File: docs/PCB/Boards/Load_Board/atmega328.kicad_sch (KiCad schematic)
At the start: 18 parts, among them J89 Conn_02x10_Odd_Even, J90 AVR-ISP-6, J91 Conn_02x10_Odd_Even, J92 Conn_01x10_Pin, J93 Conn_01x10_Pin, SW2 Tact Switch 6x6mm / 13mm, U2 ATmega328P-P, Y4 Crystal

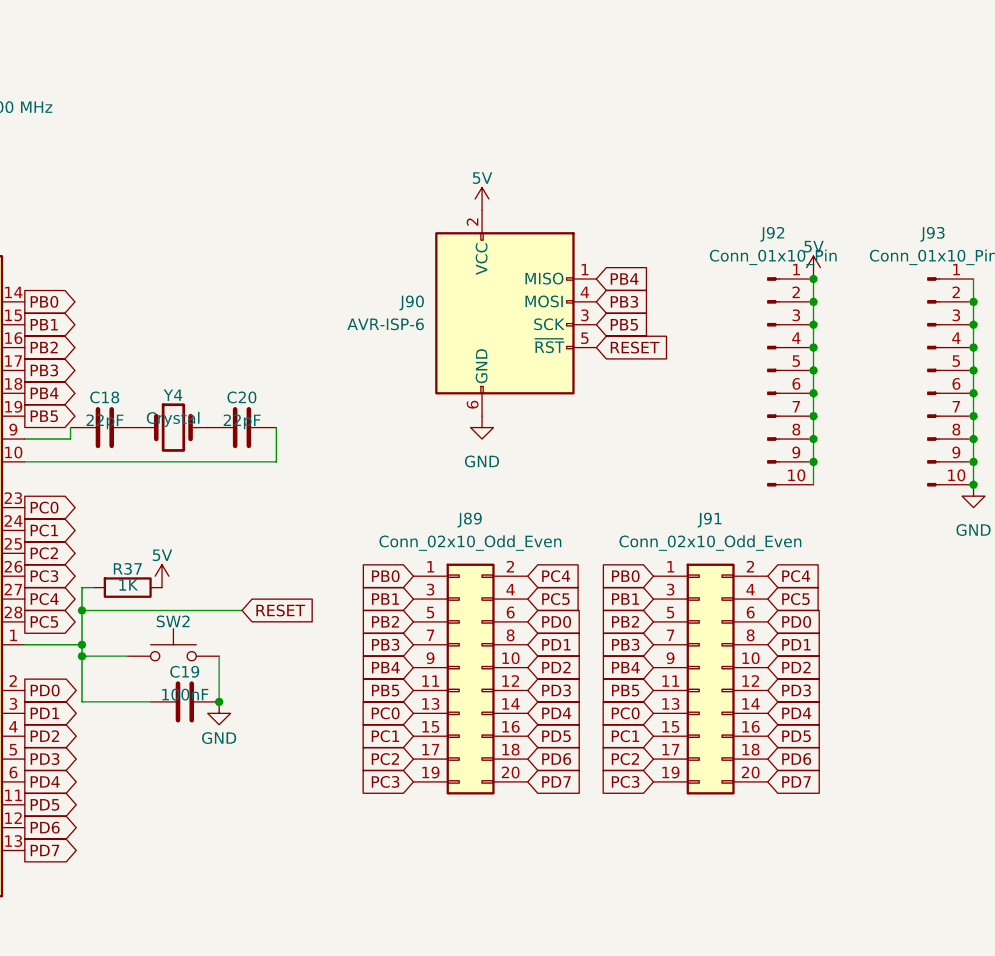
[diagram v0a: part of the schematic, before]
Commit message: Load Board updated.
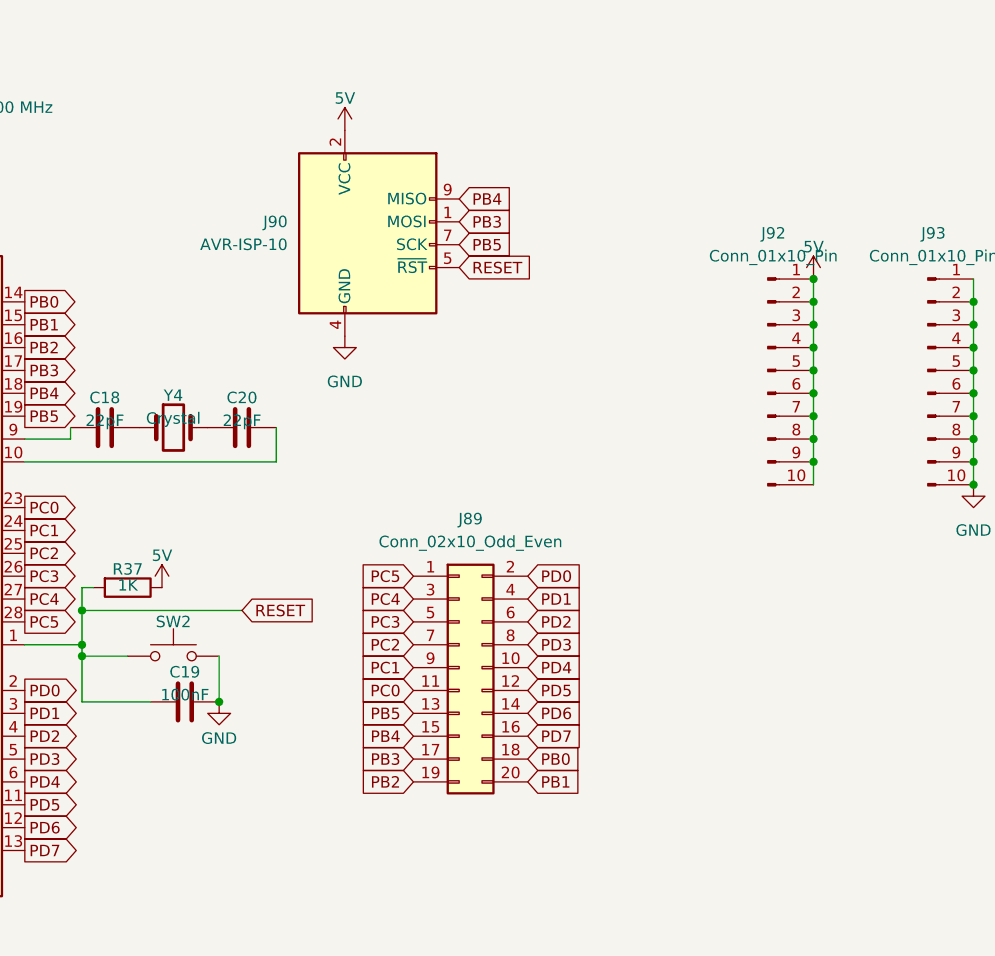
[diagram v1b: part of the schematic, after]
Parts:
- removed J90: AVR-ISP-6, Connector_IDC:IDC-Header_2x05_P2.54mm_Vertical, symbol Connector:AVR-ISP-6
- removed J91: Conn_02x10_Odd_Even, Connector_PinHeader_2.54mm:PinHeader_2x10_P2.54mm_Vertical, symbol Connector_Generic:Conn_02x10_Odd_Even
- added J90: AVR-ISP-10, Connector_IDC:IDC-Header_2x05_P2.54mm_Vertical, symbol Connector:AVR-ISP-10
- R37: footprint Resistor_THT:R_Axial_DIN0207_L6.3mm_D2.5mm_P10.16mm_Horizontal -> Resistor_SMD:R_0805_2012Metric
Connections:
- net 5V: now also J90.2 (VCC)
- net GND: now also J90.10 (GND), J90.4 (GND), J90.6 (GND), J90.8 (GND)
- net PB0: now also J89.18 (Pin_18); no longer J89.1 (Pin_1)
- net PB1: now also J89.20 (Pin_20); no longer J89.3 (Pin_3)
- net PB2: now also J89.19 (Pin_19); no longer J89.5 (Pin_5)
- net PB3: now also J89.17 (Pin_17), J90.1 (MOSI); no longer J89.7 (Pin_7)
- net PB4: now also J89.15 (Pin_15), J90.9 (MISO); no longer J89.9 (Pin_9)
- net PB5: now also J89.13 (Pin_13), J90.7 (SCK); no longer J89.11 (Pin_11)
- net PC0: now also J89.11 (Pin_11); no longer J89.13 (Pin_13)
- net PC1: now also J89.9 (Pin_9); no longer J89.15 (Pin_15)
- net PC2: now also J89.7 (Pin_7); no longer J89.17 (Pin_17)
- net PC3: now also J89.5 (Pin_5); no longer J89.19 (Pin_19)
- net PC4: now also J89.3 (Pin_3); no longer J89.2 (Pin_2)
- net PC5: now also J89.1 (Pin_1); no longer J89.4 (Pin_4)
- net PD0: now also J89.2 (Pin_2); no longer J89.6 (Pin_6)
- net PD1: now also J89.4 (Pin_4); no longer J89.8 (Pin_8)
- net PD2: now also J89.6 (Pin_6); no longer J89.10 (Pin_10)
- net PD3: now also J89.8 (Pin_8); no longer J89.12 (Pin_12)
- net PD4: now also J89.10 (Pin_10); no longer J89.14 (Pin_14)
- net PD5: now also J89.12 (Pin_12); no longer J89.16 (Pin_16)
- net PD6: now also J89.14 (Pin_14); no longer J89.18 (Pin_18)
- net PD7: now also J89.16 (Pin_16); no longer J89.20 (Pin_20)
- net RESET: now also J90.5 (~{RST})

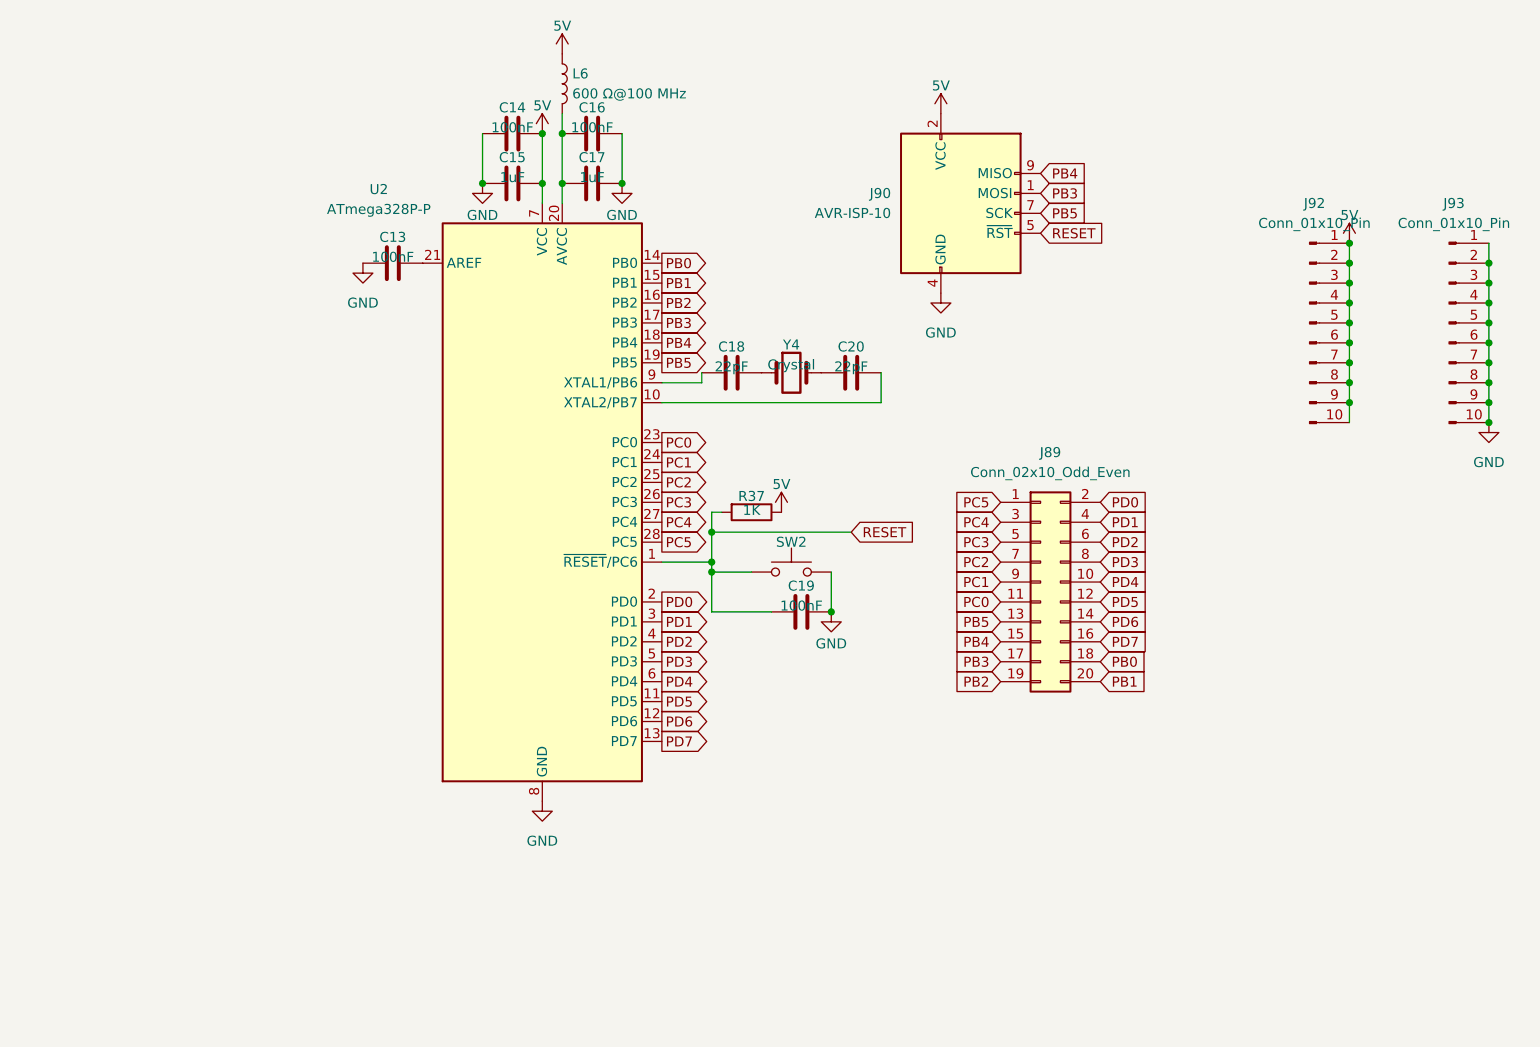
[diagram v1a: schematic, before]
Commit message: Load board and ATMega Board added
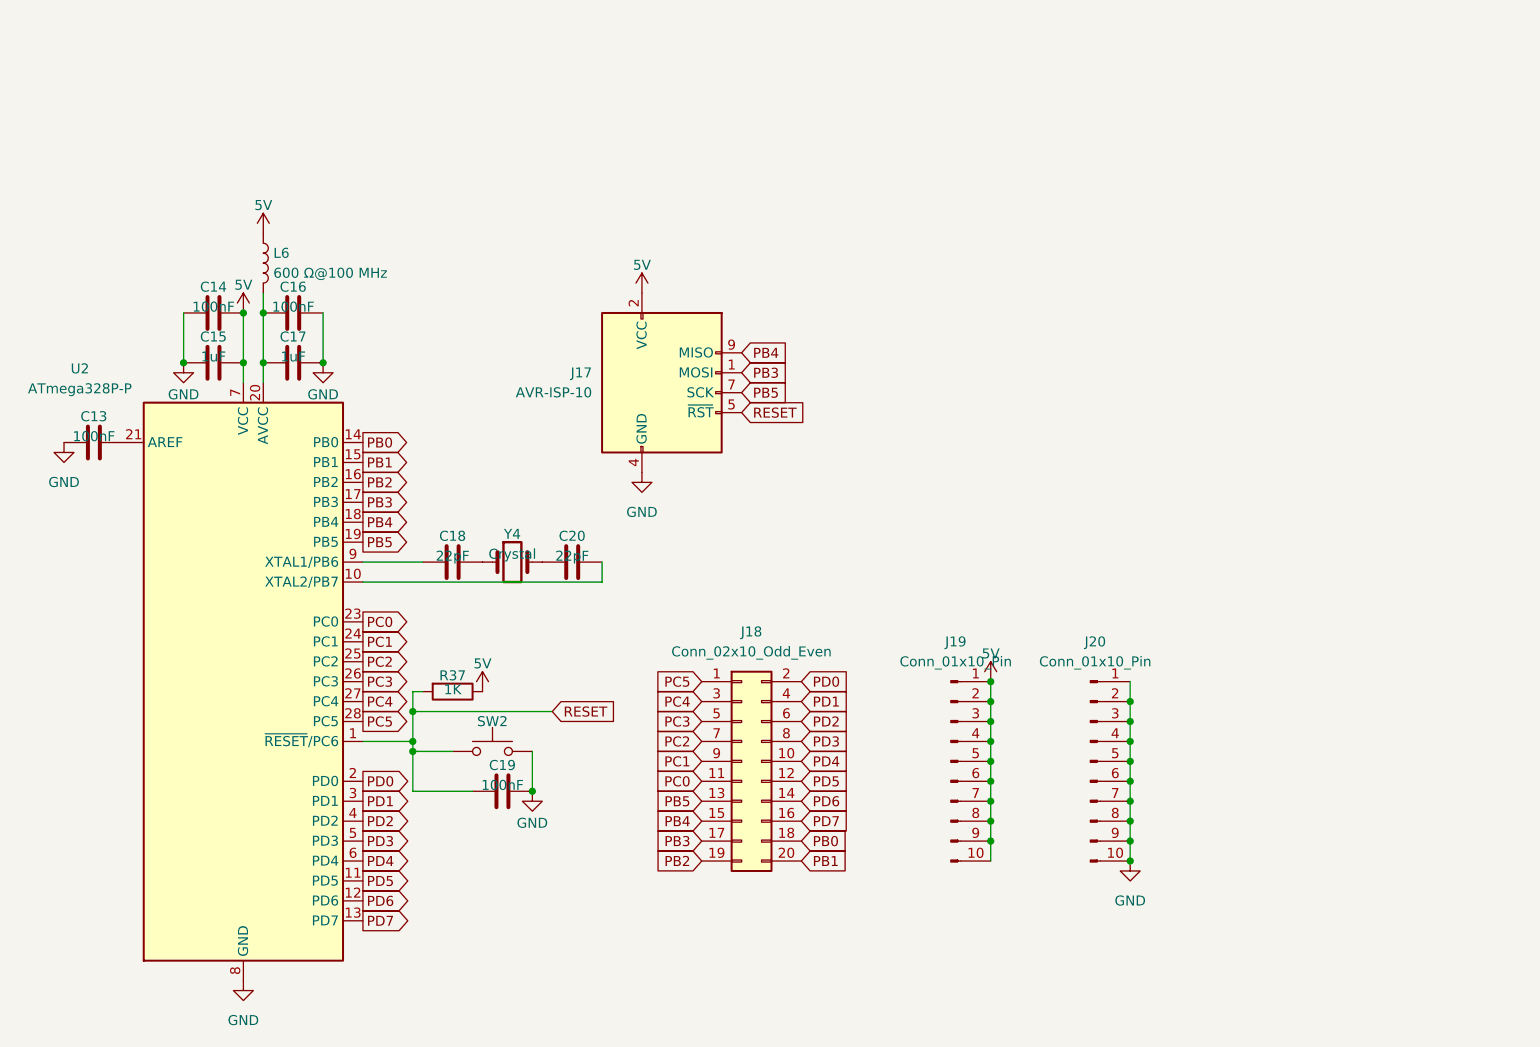
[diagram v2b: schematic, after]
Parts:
- renumbered J90 to J17, J89 to J18, J92 to J19, J93 to J20
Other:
- company: (none) -> PKl
- title: (none) -> ATMega328
- moved on the sheet: C13, C14, C15, C16, C17, C18, C19, C20, J17, J18, J19, J20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
